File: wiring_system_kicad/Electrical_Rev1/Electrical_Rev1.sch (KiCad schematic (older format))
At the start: 25 parts

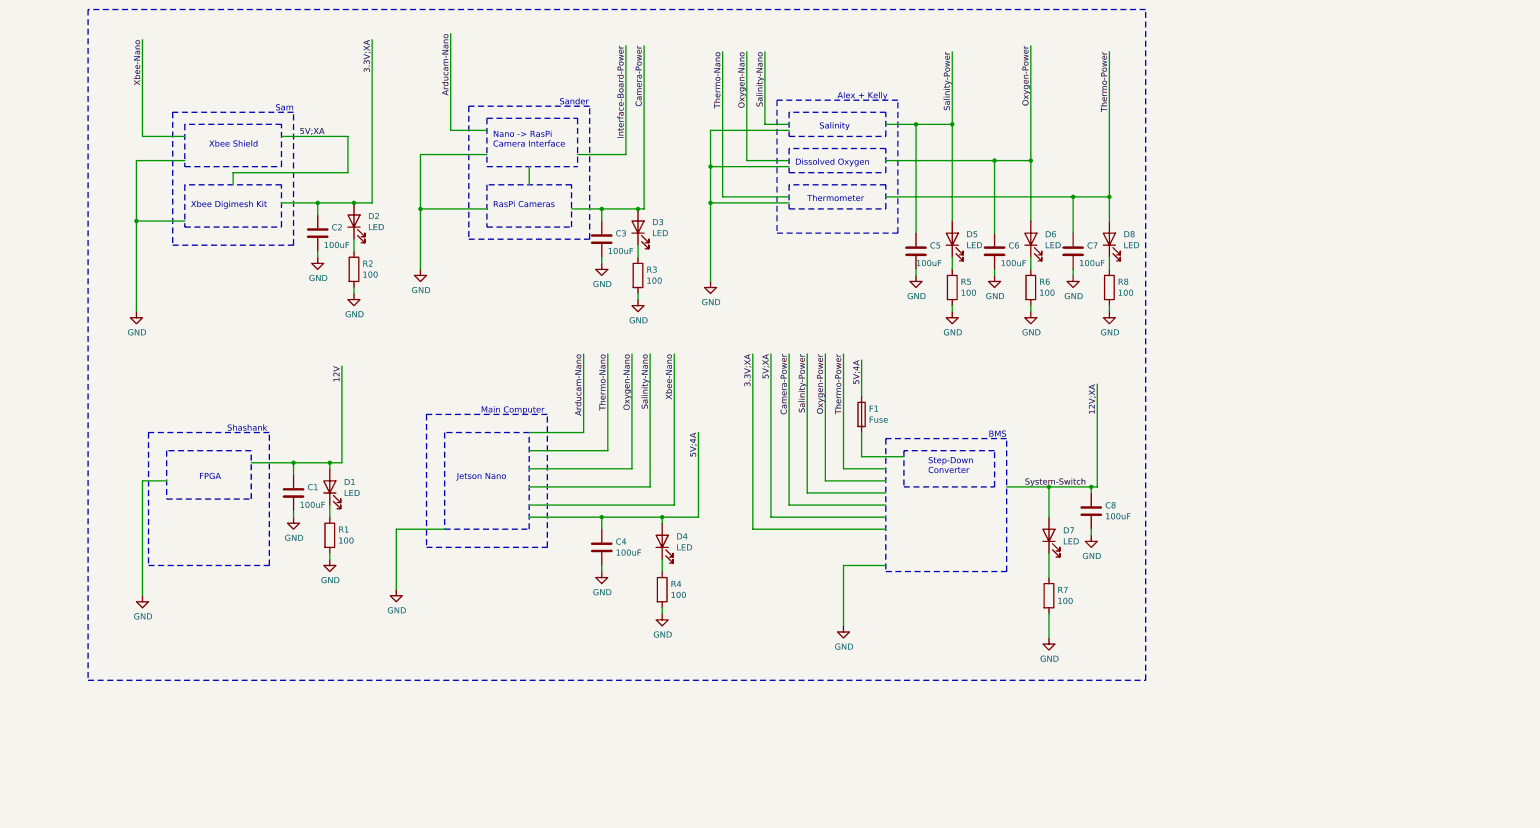
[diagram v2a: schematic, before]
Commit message: Add Fluorometer and 3.3V step down
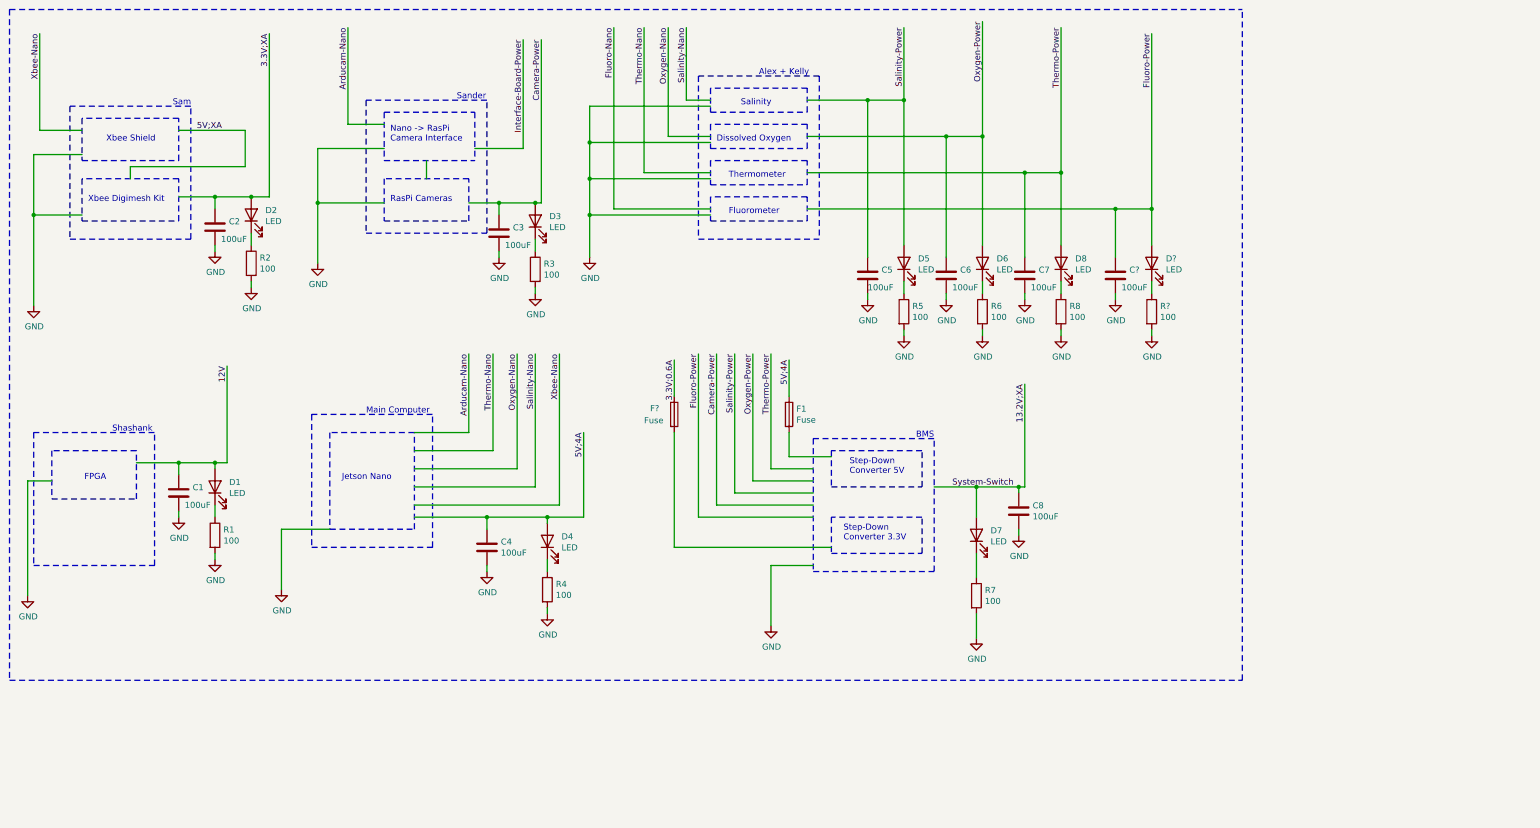
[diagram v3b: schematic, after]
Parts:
- added C?: 100uF, symbol Device:C
- added D?: LED, symbol Device:LED
- added F?: Fuse, symbol Device:Fuse
- added R?: 100, symbol Device:R
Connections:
- net labels added: 13.2V;XA, 3.3V;0.6A, Fluoro-Nano, Fluoro-Power
- net labels removed: 12V;XA
- wire segments 129 -> 142
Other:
- note added: "Fluorometer"
- note added: "Step-Down\nConverter 3.3V\n"
- note added: "Step-Down\nConverter 5V\n"
- note removed: "Step-Down\nConverter\n"
- moved on the sheet: C1, C2, C3, C4, C5, C6, C7, C8, D1, D2, D3, D4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

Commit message: Add jet drive
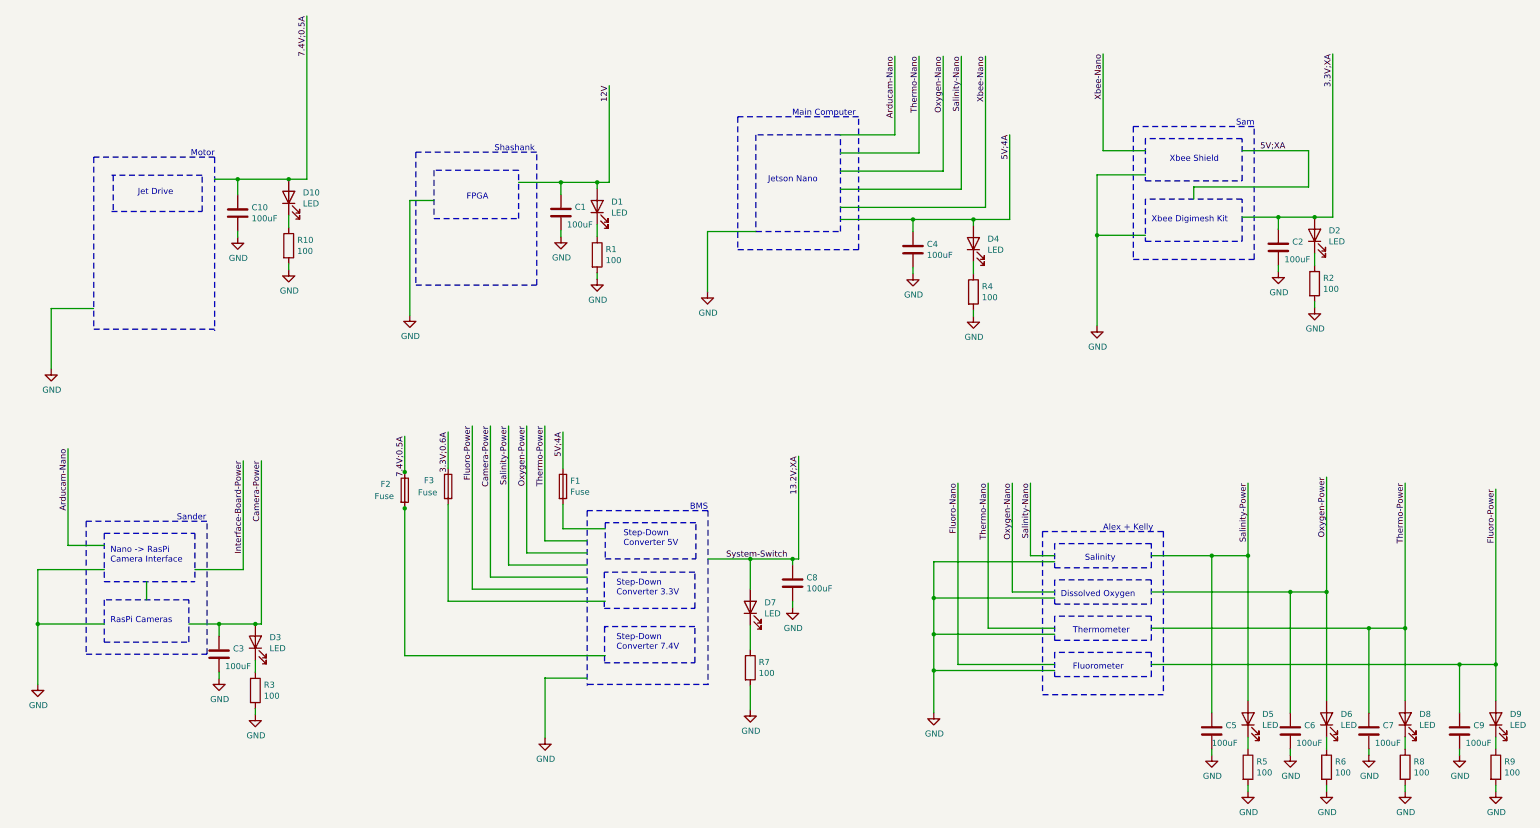
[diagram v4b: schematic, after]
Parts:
- added C10: 100uF, symbol Device:C
- added D10: LED, symbol Device:LED
- added F2: Fuse, symbol Device:Fuse
- added R10: 100, symbol Device:R
- gave numbers to parts that had none: 4
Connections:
- net labels added: 7.4V;0.5A
- wire segments 142 -> 158
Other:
- note added: "Jet Drive\n"
- note added: "Motor"
- note added: "Step-Down\nConverter 7.4V\n"
- moved on the sheet: C1, C2, C3, C4, C5, C6, C7, C8, C9, D1, D2, D3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
